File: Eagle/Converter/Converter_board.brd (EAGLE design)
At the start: 100 x 80 mm, 15 parts

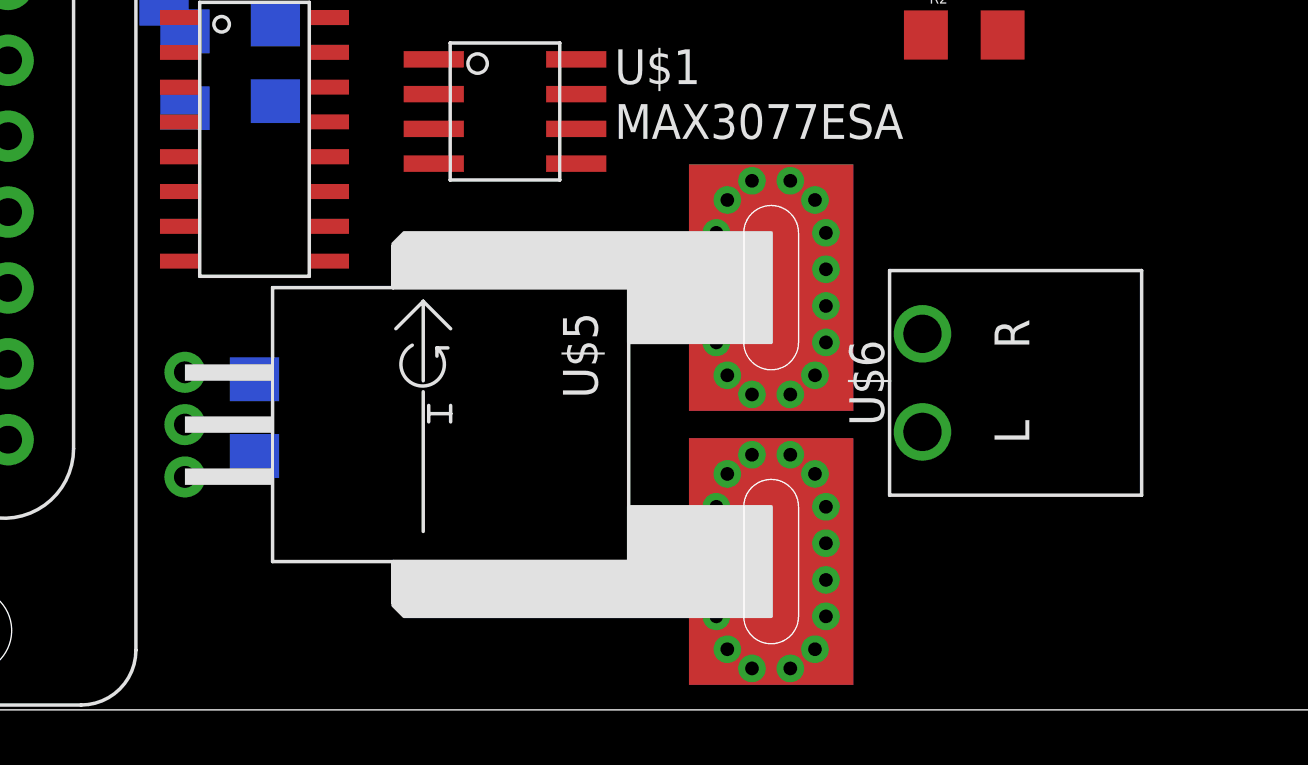
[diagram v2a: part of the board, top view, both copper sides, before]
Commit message: Removed the Current Sensor. No more Torque control.
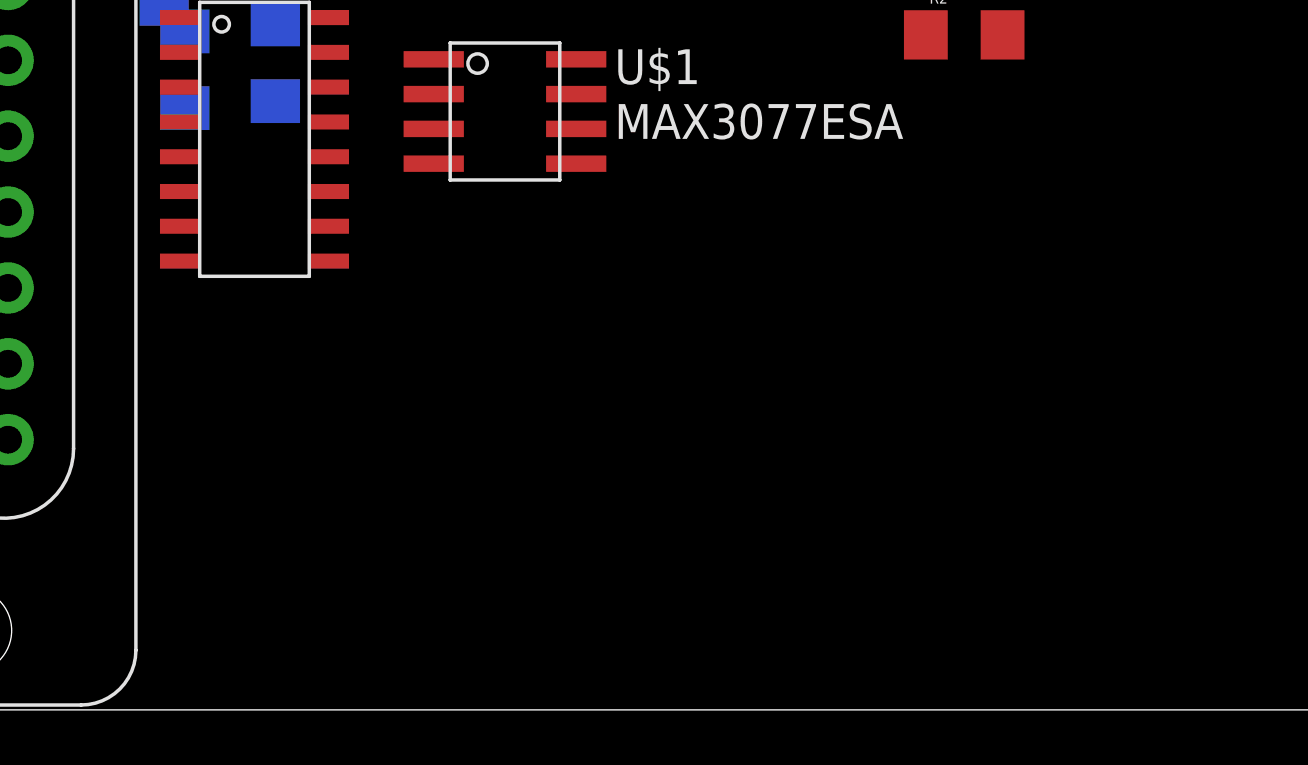
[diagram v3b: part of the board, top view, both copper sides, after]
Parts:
- removed C7: 0.1uF, SparkFun-Capacitors:1206
- removed U$5: ACS756, MRDT-2015-BMS:PFF_LEADFORM
- removed U$6: H_WR-TBL_321*0002HORIZ, MRDT-2015-PowerBoard:691322110002
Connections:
- removed net N$7: U$5.4_1, U$5.4_10, U$5.4_11, U$5.4_12, U$5.4_13, U$5.4_14, U$5.4_15, U$5.4_16, U$5.4_2, U$5.4_3, U$5.4_4, U$5.4_5, U$5.4_6, U$5.4_7, U$5.4_8, U$5.4_9, U$5.4_B, U$5.4_T, U$6.L
- removed net N$8: U$5.5_1, U$5.5_10, U$5.5_11, U$5.5_12, U$5.5_13, U$5.5_14, U$5.5_15, U$5.5_16, U$5.5_2, U$5.5_3, U$5.5_4, U$5.5_5, U$5.5_6, U$5.5_7, U$5.5_8, U$5.5_9, U$5.5_B, U$5.5_T, U$6.R
- net ANA1: no longer U$5.3
- net GND: no longer C7.2, U$5.2
- net VCC: no longer C7.1, U$5.1
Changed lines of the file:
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@@
 <element name="U$3" library="MRDT-LIB2014" package="RJ45-CAT5E" value="RJ45" x="22.606" y="35.306" rot="R180"/>
 <element name="U$4" library="MRDT-LIB2014" package="DB15" value="DB15" x="6.096" y="19.558" rot="R270"/>
-<element name="U$5" library="MRDT-2015-BMS" package="PFF_LEADFORM" value="ACS756" x="13.97" y="10.414" rot="R270"/>
 <element name="R1" library="SparkFun-Passives" package="1206" value="120" x="54.864" y="27.432"/>
 <element name="R2" library="SparkFun-Passives" package="1206" value="120" x="42.418" y="24.638"/>
-<element name="C7" library="SparkFun-Capacitors" package="1206" value="0.1uF" x="16.51" y="10.668" rot="MR270"/>
-<element name="U$6" library="MRDT-2015-PowerBoard" package="691322110002" value="H_WR-TBL_321*0002HORIZ" x="40.894" y="11.938" rot="R90">
-<attribute name="DIGIKEY_PN" value="732-2769-ND" x="40.894" y="11.938" size="1.778" layer="27" rot="R90" display="off"/>
-</element>
 </elements>
 <signals>
@@
 <contactref element="U$4" pad="13"/>
 <contactref element="U$4" pad="5"/>
-<contactref element="U$5" pad="2"/>
-<contactref element="C7" pad="2"/>
-<wire x1="42.04" y1="36.576" x2="35.56" y2="33.652" width="0" layer="19" extent="1-1"/>
-<wire x1="23.054" y1="19.939" x2="42.04" y2="36.576" width="0" layer="19" extent="1-1"/>
-<wire x1="19.304" y1="28.318" x2="23.054" y2="19.939" width="0" layer="19" extent="1-1"/>
-<wire x1="19.21" y1="24.003" x2="19.304" y2="28.318" width="0" layer="19" extent="1-1"/>
-<wire x1="17.272" y1="25.022" x2="19.21" y2="24.003" width="0" layer="19" extent="1-1"/>
-<wire x1="18.161" y1="28.111" x2="17.272" y2="25.022" width="0" layer="19" extent="1-1"/>
-<wire x1="19.431" y1="30.651" x2="18.161" y2="28.111" width="0" layer="19" extent="1-1"/>
-<wire x1="4.676" y1="22.328" x2="17.272" y2="25.022" width="0" layer="19" extent="1-1"/>
-<wire x1="7.516" y1="18.173" x2="4.676" y2="22.328" width="0" layer="19" extent="1-1"/>
-<wire x1="16.51" y1="9.268" x2="7.516" y2="18.173" width="0" layer="19" extent="1-1"/>
-<wire x1="13.97" y1="10.414" x2="16.51" y2="9.268" width="0" layer="19" extent="1-1"/>
+<wire x1="35.56" y1="33.652" x2="42.04" y2="36.576" width="0" layer="19" extent="1-1"/>
+<wire x1="19.431" y1="30.651" x2="35.56" y2="33.652" width="0" layer="19" extent="1-1"/>
+<wire x1="19.304" y1="28.318" x2="19.431" y2="30.651" width="0" layer="19" extent="1-1"/>
+<wire x1="18.161" y1="28.111" x2="19.304" y2="28.318" width="0" layer="19" extent="1-1"/>
+<wire x1="17.272" y1="25.022" x2="18.161" y2="28.111" width="0" layer="19" extent="16-16"/>
+<wire x1="19.21" y1="24.003" x2="17.272" y2="25.022" width="0" layer="19" extent="1-16"/>
+<wire x1="23.054" y1="19.939" x2="19.21" y2="24.003" width="0" layer="19" extent="1-1"/>
+<wire x1="7.516" y1="18.173" x2="17.272" y2="25.022" width="0" layer="19" extent="16-16"/>
+<wire x1="4.676" y1="22.328" x2="7.516" y2="18.173" width="0" layer="19" extent="1-1"/>
 </signal>
 <signal name="VCC">
@@
 <contactref element="U$3" pad="5"/>
 <contactref element="U$4" pad="14"/>
-<contactref element="U$5" pad="1"/>
-<contactref element="C7" pad="1"/>
+<wire x1="23.241" y1="28.111" x2="39.24" y2="36.576" width="0" layer="19" extent="1-1"/>
 <wire x1="21.971" y1="30.651" x2="23.241" y2="28.111" width="0" layer="19" extent="1-1"/>
-<wire x1="19.304" y1="31.118" x2="23.241" y2="28.111" width="0" layer="19" extent="1-1"/>
-<wire x1="39.24" y1="36.576" x2="19.304" y2="31.118" width="0" layer="19" extent="1-1"/>
-<wire x1="23.054" y1="23.749" x2="39.24" y2="36.576" width="0" layer="19" extent="1-1"/>
-<wire x1="19.21" y1="25.273" x2="19.304" y2="31.118" width="0" layer="19" extent="1-1"/>
-<wire x1="13.97" y1="12.324" x2="19.21" y2="25.273" width="0" layer="19" extent="1-1"/>
-<wire x1="16.51" y1="12.068" x2="13.97" y2="12.324" width="0" layer="19" extent="1-1"/>
+<wire x1="19.304" y1="31.118" x2="21.971" y2="30.651" width="0" layer="19" extent="1-1"/>
+<wire x1="23.054" y1="23.749" x2="23.241" y2="28.111" width="0" layer="19" extent="1-1"/>
+<wire x1="19.21" y1="25.273" x2="23.054" y2="23.749" width="0" layer="19" extent="1-1"/>
 <wire x1="4.676" y1="25.098" x2="19.21" y2="25.273" width="0" layer="19" extent="1-1"/>
 </signal>
@@
 <signal name="ANA1">
 <contactref element="U$4" pad="4"/>
-<contactref element="U$5" pad="3"/>
-<wire x1="13.97" y1="8.504" x2="7.516" y2="20.943" width="0" layer="19" extent="1-1"/>
-</signal>
-<signal name="N$7">
-<contactref element="U$5" pad="4_2" route="any" routetag="G$1.IP+"/>
-<contactref element="U$5" pad="4_16" route="any" routetag="G$1.IP+"/>
-<contactref element="U$5" pad="4_10" route="any" routetag="G$1.IP+"/>
-<contactref element="U$5" pad="4_1" route="any" routetag="G$1.IP+"/>
-<contactref element="U$5" pad="4_6" route="any" routetag="G$1.IP+"/>
-<contactref element="U$5" pad="4_5" route="any" routetag="G$1.IP+"/>
-<contactref element="U$5" pad="4_4" route="any" routetag="G$1.IP+"/>
-<contactref element="U$5" pad="4_T" route="any" routetag="G$1.IP+"/>
-<contactref element="U$5" pad="4_13" route="any" routetag="G$1.IP+"/>
-<contactref element="U$5" pad="4_12" route="any" routetag="G$1.IP+"/>
-<contactref element="U$5" pad="4_14" route="any" routetag="G$1.IP+"/>
-<contactref element="U$5" pad="4_9" route="any" routetag="G$1.IP+"/>
-<contactref element="U$5" pad="4_8" route="any" routetag="G$1.IP+"/>
-<contactref element="U$5" pad="4_11" route="any" routetag="G$1.IP+"/>
-<contactref element="U$5" pad="4_B" route="any" routetag="G$1.IP+"/>
-<contactref element="U$5" pad="4_3" route="any" routetag="G$1.IP+"/>
-<contactref element="U$5" pad="4_15" route="any" routetag="G$1.IP+"/>
-<contactref element="U$5" pad="4_7" route="any" routetag="G$1.IP+"/>
-<contactref element="U$6" pad="L"/>
-<wire x1="36.07" y1="9.314" x2="40.894" y2="10.148" width="0" layer="19" extent="1-1"/>
-</signal>
-<signal name="N$8">
-<contactref element="U$5" pad="5_1" route="any" routetag="G$1.IP-"/>
-<contactref element="U$5" pad="5_4" route="any" routetag="G$1.IP-"/>
-<contactref element="U$5" pad="5_7" route="any" routetag="G$1.IP-"/>
-<contactref element="U$5" pad="5_T" route="any" routetag="G$1.IP-"/>
-<contactref element="U$5" pad="5_2" route="any" routetag="G$1.IP-"/>
-<contactref element="U$5" pad="5_13" route="any" routetag="G$1.IP-"/>
-<contactref element="U$5" pad="5_B" route="any" routetag="G$1.IP-"/>
-<contactref element="U$5" pad="5_10" route="any" routetag="G$1.IP-"/>
-<contactref element="U$5" pad="5_16" route="any" routetag="G$1.IP-"/>
-<contactref element="U$5" pad="5_3" route="any" routetag="G$1.IP-"/>
-<contactref element="U$5" pad="5_11" route="any" routetag="G$1.IP-"/>
-<contactref element="U$5" pad="5_15" route="any" routetag="G$1.IP-"/>
-<contactref element="U$5" pad="5_5" route="any" routetag="G$1.IP-"/>
-<contactref element="U$5" pad="5_9" route="any" routetag="G$1.IP-"/>
-<contactref element="U$5" pad="5_12" route="any" routetag="G$1.IP-"/>
-<contactref element="U$5" pad="5_6" route="any" routetag="G$1.IP-"/>
-<contactref element="U$5" pad="5_8" route="any" routetag="G$1.IP-"/>
-<contactref element="U$5" pad="5_14" route="any" routetag="G$1.IP-"/>
-<contactref element="U$6" pad="R"/>
-<wire x1="34.67" y1="19.314" x2="40.894" y2="13.728" width="0" layer="19" extent="1-1"/>
 </signal>
 </signals>

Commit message: routed board
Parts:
- moved R1 34.9 mm to (20.6, 20.8), turned to 270 degrees
- moved R2 28.2 mm to (14.7, 19.1), turned to 180 degrees
- moved U$3 26.2 mm to (20.6, 9.14), turned to 90 degrees
- moved C6 22.5 mm to (24.6, 20.8), turned to 90 degrees
- moved C2 13.4 mm to (20.6, 35.1), flipped to the top, turned to 90 degrees
- moved U$2 13.0 mm to (16.0, 33.8), turned to 180 degrees
- moved C4 12.0 mm to (24.6, 30.0)
- moved U$1 10.3 mm to (15.7, 24.6), turned to 270 degrees
- moved C5 9.48 mm to (22.6, 20.8), turned to 90 degrees
- moved C3 8.29 mm to (22.6, 30.0), flipped to the top, turned to 270 degrees
- moved C1 7.88 mm to (20.6, 30.0), flipped to the top, turned to 90 degrees
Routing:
- net TRANS-: track 0.00 -> 28.7 mm
- net TRANS+: track 0.00 -> 22.0 mm
- net VCC: track 0.00 -> 21.5 mm, vias 0 -> 3
- net GND: track 0.00 -> 20.1 mm, vias 0 -> 2
- net REC+: track 0.00 -> 19.1 mm
- net REC-: track 0.00 -> 15.1 mm
- net T_IN1: track 0.00 -> 13.7 mm
- net R_OUT1: track 0.00 -> 13.5 mm
- net N$5: track 0.00 -> 8.32 mm
- net R_IN1: track 0.00 -> 7.50 mm
- net N$4: track 0.00 -> 6.24 mm
- net T_OUT1: track 0.00 -> 5.85 mm
- net N$6: track 0.00 -> 5.24 mm
- net N$2: track 0.00 -> 2.19 mm
- net N$3: track 0.00 -> 2.08 mm
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- added copper zone on layer 16, net GND
- added copper zone on layer 1, net VCC
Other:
- board size 100 x 80 mm -> 28.9 x 39.6 mm

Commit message: cleaned up comm board
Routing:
- net VCC: track 21.5 -> 9.00 mm, vias 3 -> 1
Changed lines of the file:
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@@
 <wire x1="22.606" y1="22.228" x2="24.638" y2="22.228" width="1.4224" layer="1"/>
 <wire x1="24.638" y1="28.572" x2="22.606" y2="28.572" width="1.4224" layer="1"/>
-<wire x1="24.638" y1="22.228" x2="24.638" y2="26.416" width="1.4224" layer="1"/>
-<via x="24.638" y="26.416" extent="1-16" drill="0.6" diameter="1.4224"/>
-<wire x1="24.638" y1="26.416" x2="25.654" y2="26.416" width="1.4224" layer="16"/>
-<wire x1="24.638" y1="28.572" x2="24.638" y2="26.416" width="1.4224" layer="1"/>
+<wire x1="24.638" y1="22.228" x2="24.638" y2="25.4" width="1.4224" layer="1"/>
+<via x="24.638" y="25.4" extent="1-16" drill="0.6" diameter="1.4224"/>
+<wire x1="24.638" y1="25.4" x2="25.654" y2="26.416" width="1.4224" layer="16"/>
+<wire x1="24.638" y1="28.572" x2="24.638" y2="25.4" width="1.4224" layer="1"/>
 <wire x1="13.302" y1="30.607" x2="10.668" y2="30.607" width="0.4064" layer="1"/>
 <via x="10.668" y="30.607" extent="1-16" drill="0.6" diameter="1.4224"/>
@@
 <via x="19.558" y="9.906" extent="1-16" drill="0.6" diameter="1.4224"/>
 <wire x1="19.558" y1="9.906" x2="19.812" y2="9.906" width="1.4224" layer="1"/>
-<wire x1="17.653" y1="27.238" x2="18.99" y2="27.238" width="1.4224" layer="1"/>
-<wire x1="18.99" y1="27.238" x2="19.05" y2="27.178" width="1.4224" layer="1"/>
-<wire x1="19.05" y1="27.178" x2="19.05" y2="25.654" width="1.4224" layer="1"/>
-<wire x1="19.05" y1="25.654" x2="21.336" y2="25.654" width="1.4224" layer="1"/>
-<wire x1="21.336" y1="25.654" x2="22.606" y2="24.384" width="1.4224" layer="1"/>
-<via x="22.606" y="24.384" extent="1-16" drill="0.6" diameter="1.4224"/>
-<wire x1="22.606" y1="24.384" x2="26.67" y2="24.384" width="1.4224" layer="16"/>
-<via x="26.67" y="24.384" extent="1-16" drill="0.6" diameter="1.4224"/>
-<wire x1="26.67" y1="24.384" x2="26.67" y2="23.368" width="1.4224" layer="1"/>
-<wire x1="26.67" y1="23.368" x2="26.924" y2="23.114" width="1.4224" layer="1"/>
 <wire x1="13.302" y1="29.337" x2="12.573" y2="29.337" width="0.4064" layer="1"/>
 <wire x1="12.573" y1="29.337" x2="11.684" y2="28.448" width="0.4064" layer="1"/>

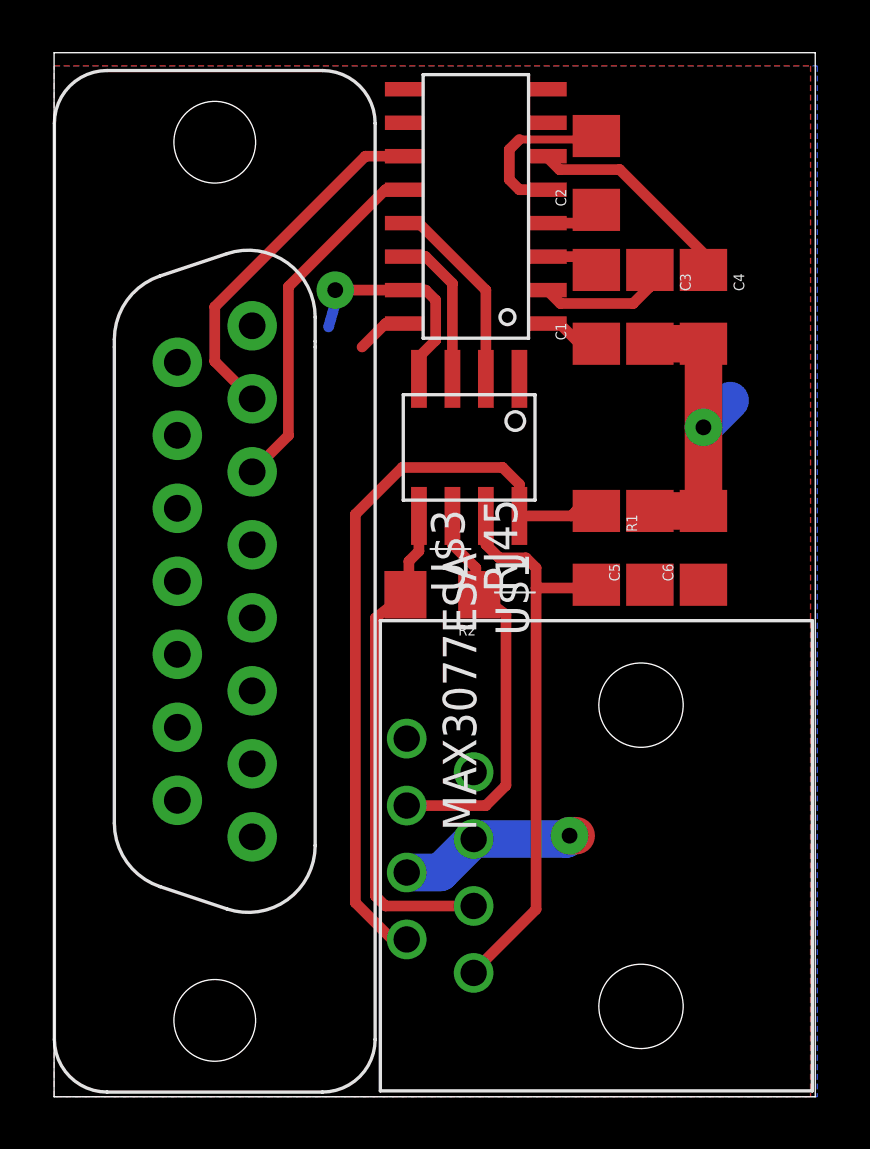
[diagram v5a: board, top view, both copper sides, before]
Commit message: added bom
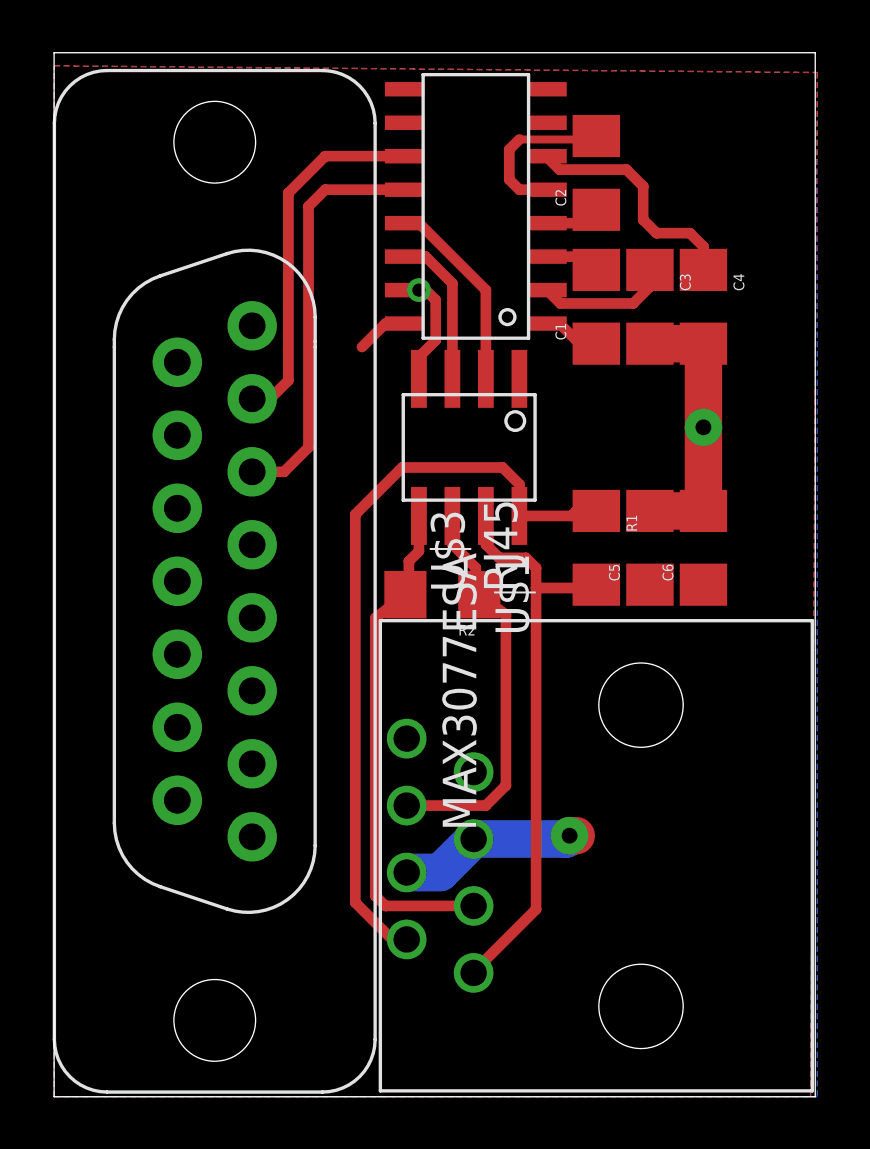
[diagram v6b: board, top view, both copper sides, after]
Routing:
- net GND: track 20.5 -> 15.0 mm
- net R_OUT1: track 13.5 -> 15.6 mm
- net N$5: track 8.32 -> 9.01 mm

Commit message: rerouted board
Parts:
- moved R1 16.1 mm to (18.5, 4.83), flipped to the bottom
- moved R2 10.1 mm to (18.5, 9.65), flipped to the bottom, turned to 270 degrees
- moved C2 5.24 mm to (22.6, 30.2)
- moved U$2 4.60 mm to (16.5, 29.2)
- moved C3 4.57 mm to (22.6, 25.4)
- moved C4 4.57 mm to (24.6, 25.4)
- moved C1 4.07 mm to (24.6, 30.2)
- moved U$1 3.64 mm to (16.5, 21.1), turned to 0 degrees
- moved C5 2.05 mm to (24.6, 20.6)
- moved C6 2.05 mm to (22.6, 20.6)
- moved U$3 0.20 mm to (20.6, 8.95)
- moved U$4 0.14 mm to (6.16, 19.4), flipped to the bottom, turned to 90 degrees
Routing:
- net N$1: track 2.08 -> 17.5 mm
- net T_IN1: track 13.8 -> 24.9 mm, vias 0 -> 1
- net N$2: track 2.19 -> 11.5 mm
- net VCC: track 9.00 -> 0.00 mm, vias 1 -> 0
- net T_OUT1: track 5.85 -> 9.96 mm, vias 0 -> 2
- net R_OUT1: track 15.6 -> 19.7 mm
- net TRANS-: track 28.7 -> 24.8 mm, vias 0 -> 1
- net TRANS+: track 22.0 -> 24.8 mm
- net R_IN1: track 7.50 -> 9.96 mm
- net N$5: track 9.01 -> 11.0 mm, vias 0 -> 2
- net REC+: track 19.1 -> 17.3 mm
- net N$4: track 6.24 -> 4.69 mm
- net N$6: track 5.24 -> 3.71 mm
- net N$3: track 2.08 -> 3.50 mm
- net GND: track 15.0 -> 14.3 mm, vias 2 -> 3
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- added copper zone on layer 1, net GND
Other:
- board size 28.9 x 39.6 mm -> 28.4 x 38.9 mm
